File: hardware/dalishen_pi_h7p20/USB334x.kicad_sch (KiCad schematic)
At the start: 29 parts, among them J2 USB_C_Receptacle_USB2.0_16P, J3 USB_A, U18 LM2903, U19 LM2903, U2 LM2903, U20 USB3343, Y1 26M,NC

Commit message: [dalishen_pi_h7p20] backup
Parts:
- removed C2: 0.1uF, Capacitor_SMD:C_0402_1005Metric, symbol Device:C
- removed D5, D6: 1N5819(S4), vllogic:D_SOD-323_BAT60, symbol Device:D_Schottky
- removed R11: 0, Resistor_SMD:R_0402_1005Metric, symbol Device:R
- removed R88: 33, Resistor_SMD:R_0402_1005Metric, symbol Device:R
- C12, C14: value 20pF,NC -> 9pF
- J2: footprint Connector_USB:USB_C_Receptacle_GCT_USB4105-xx-A_16P_TopMnt_Horizontal -> vllogic:USB_C_Receptacle_16P
- J3: footprint vllogic:USB-AF-180 -> vllogic:USB-AF_YIJIAN
- R1, R79, R90: value 10k -> 10k,1%
- R78: value 1M,NC -> 1M
- U18, U19, U2: value LM2903 -> LM2903A-VR
- Y1: value 26M,NC -> 26M
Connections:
- net GND: now also J2.S1 (SHIELD), J3.5 (Shield)
- net VCC_3V3: now also R90.1; no longer C1.2, U18.8 (V+), U19.8 (V+), U2.8 (V+)
- net VCC_5V: now also C1.2, U18.8 (V+), U19.8 (V+), U2.8 (V+)
- net at C50.2, U20.15 (VDD33), U20.18 (ID): no longer R90.1

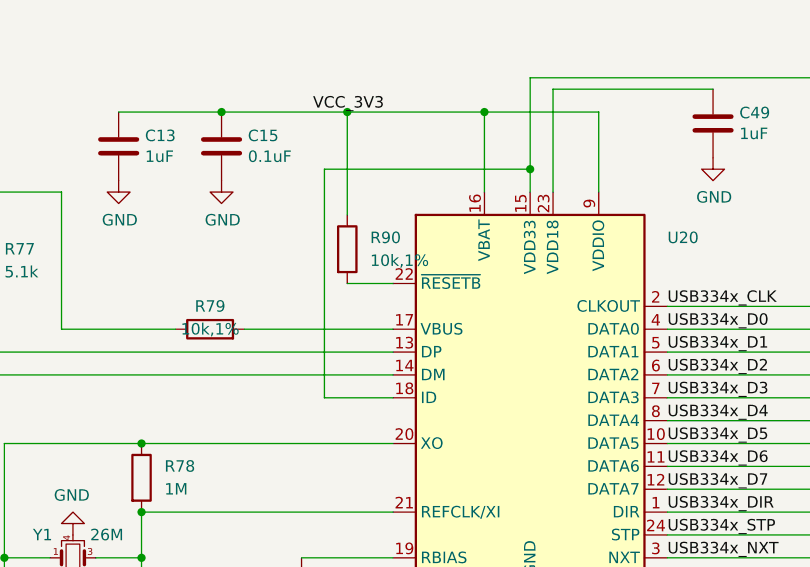
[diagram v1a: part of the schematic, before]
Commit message: [dalishen_pi_h7p20] 原理图初稿
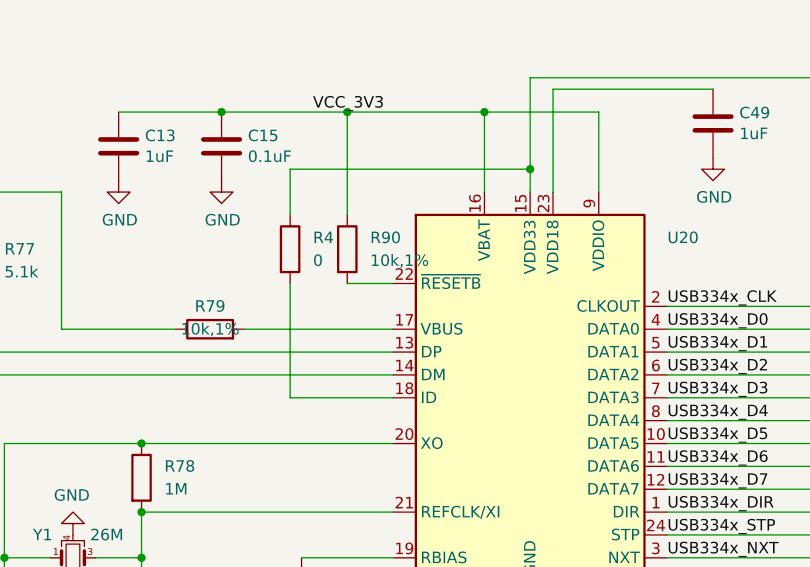
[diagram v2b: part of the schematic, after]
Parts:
- added R4: 0, Resistor_SMD:R_0402_1005Metric, symbol Device:R
- Y1: footprint vllogic:OSC_3225 -> vllogic:OSC_2016
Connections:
- net at C50.2, U20.15 (VDD33): now also R4.1; no longer U20.18 (ID)
- new net: R4.2, U20.18 (ID)
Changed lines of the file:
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@@
+    (stroke (width 0) (type default))
+  )
+  (wire (pts (xy 171.45 63.5) (xy 171.45 76.2))
     (stroke (width 0) (type default))
   )
@@
     (stroke (width 0) (type default))
   )
-  (wire (pts (xy 175.26 76.2) (xy 182.88 76.2))
+  (wire (pts (xy 171.45 76.2) (xy 182.88 76.2))
     (stroke (width 0) (type default))
   )
@@
     (stroke (width 0) (type default))
   )
-  (wire (pts (xy 175.26 50.8) (xy 175.26 76.2))
+  (wire (pts (xy 171.45 50.8) (xy 171.45 55.88))
     (stroke (width 0) (type default))
   )
@@
     (stroke (width 0) (type default))
   )
-  (wire (pts (xy 175.26 50.8) (xy 198.12 50.8))
+  (wire (pts (xy 171.45 50.8) (xy 198.12 50.8))
     (stroke (width 0) (type default))
   )
@@
     )
   )
+  (symbol (lib_id "Device:R") (at 171.45 59.69 0) (unit 1)
+    (in_bom yes) (on_board yes) (dnp no) (fields_autoplaced)
+    (property "Reference" "R4" (at 173.99 58.42 0)
+      (effects (font (size 1.27 1.27)) (justify left))
+    )
+    (property "Value" "0" (at 173.99 60.96 0)
+      (effects (font (size 1.27 1.27)) (justify left))
+    )
+    (property "Footprint" "Resistor_SMD:R_0402_1005Metric" (at 169.672 59.69 90)
+      (effects (font (size 1.27 1.27)) hide)
+    )
+    (property "Datasheet" "~" (at 171.45 59.69 0)
+      (effects (font (size 1.27 1.27)) hide)
+    )
+    (pin "2")
+    (pin "1")
+    (instances
+      (project "dalishen_pi_h7p20"
+        (path "/221176f3-b6da-4f04-afa6-f8c6dd49907a/c2e39904-e110-4fb2-9a78-c219110dbd62"
+          (reference "R4") (unit 1)
+        )
+      )
+    )
+  )
   (symbol (lib_id "power:GND") (at 24.13 125.73 0) (unit 1)
     (in_bom yes) (on_board yes) (dnp no)
@@
       (effects (font (size 1.27 1.27)) (justify left))
     )
-    (property "Footprint" "vllogic:OSC_3225" (at 147.32 93.98 0)
-      (effects (font (size 1.27 1.27)) hide)
-    )
+    (property "Footprint" "vllogic:OSC_2016" (at 147.32 93.98 0)
+      (effects (font (size 1.27 1.27)) hide)
+    )

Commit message: [dalishen_pi_h7p20] 原理图预审
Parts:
- C12, C14: value 9pF -> 4.3pF
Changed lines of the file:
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@@
       (effects (font (size 1.27 1.27)) (justify right))
     )
-    (property "Value" "9pF" (at 142.621 100.203 0)
+    (property "Value" "4.3pF" (at 142.621 100.203 0)
       (effects (font (size 1.27 1.27)) (justify right))
     )
@@
       (effects (font (size 1.27 1.27)) (justify right))
     )
-    (property "Value" "9pF" (at 157.861 100.203 0)
-      (effects (font (size 1.27 1.27)) (justify right))
-    )
+    (property "Value" "4.3pF" (at 157.861 100.203 0)
+      (effects (font (size 1.27 1.27)) (justify right))
+    )

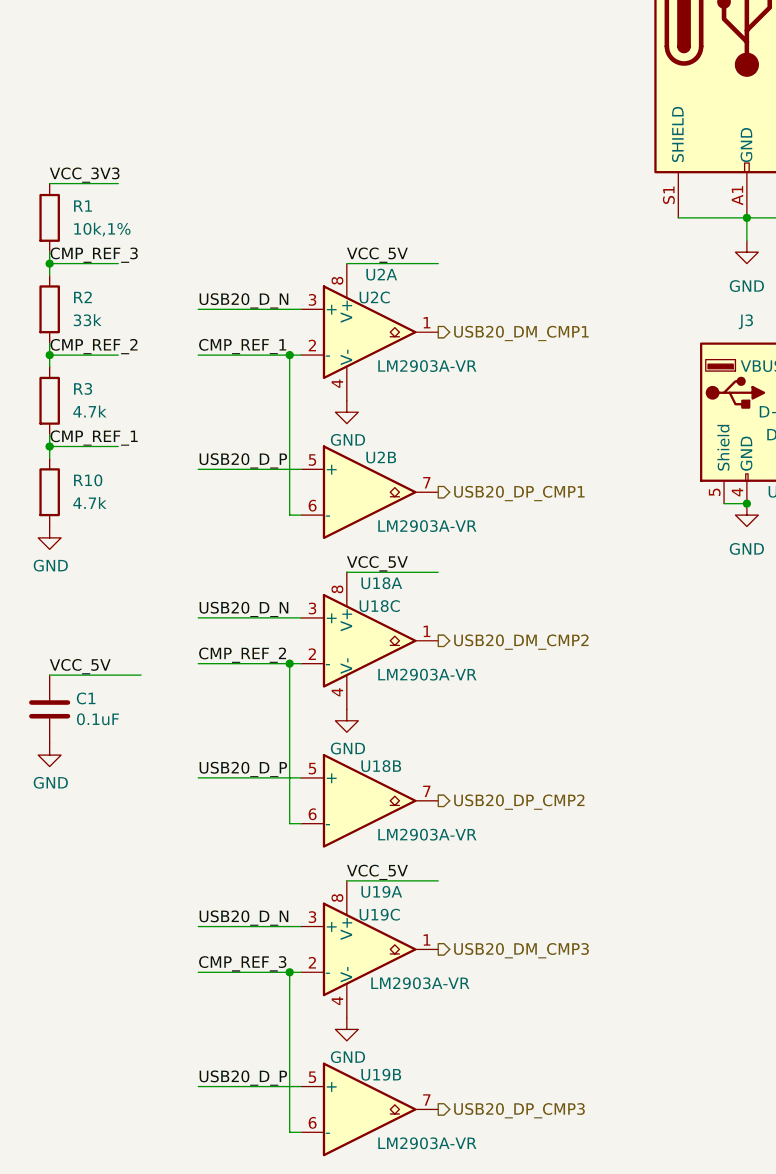
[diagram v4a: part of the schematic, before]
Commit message: [dalishen_pi_h7p20] 由于JTAG口在LQFP128封装上无法作为IO使用，故移除SE0，J, K状态电路
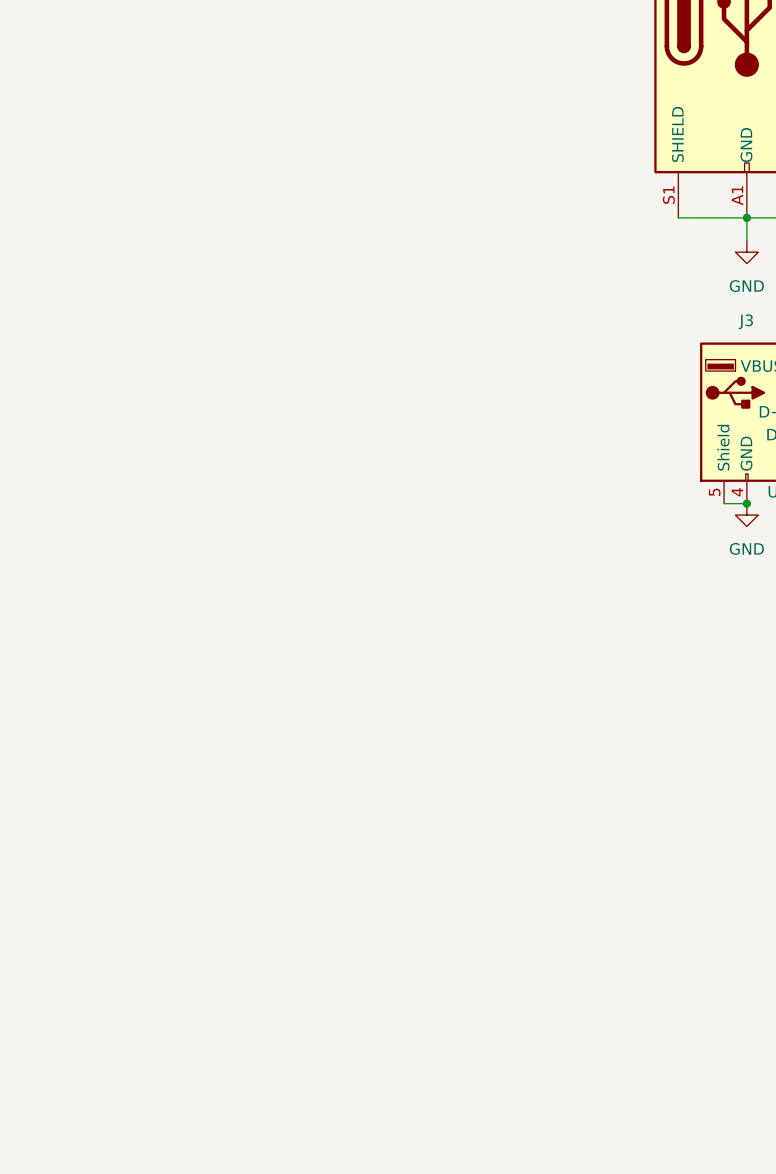
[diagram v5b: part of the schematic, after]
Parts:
- removed C1: 0.1uF, Capacitor_SMD:C_0402_1005Metric, symbol Device:C
- removed R1: 10k,1%, Resistor_SMD:R_0402_1005Metric, symbol Device:R
- removed R10, R3: 4.7k, Resistor_SMD:R_0402_1005Metric, symbol Device:R
- removed R2: 33k, Resistor_SMD:R_0402_1005Metric, symbol Device:R
- removed U18, U19, U2: LM2903A-VR, Package_SO:MSOP-8_3x3mm_P0.65mm, symbol Comparator:LM2903

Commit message: [dalishen_pi_h7p20] A母换SMT型号
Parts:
- J3: footprint vllogic:USB-AF_YIJIAN -> vllogic:USB_AF_SMT
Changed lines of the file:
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@@
 			)
 		)
-		(property "Footprint" "vllogic:USB-AF_YIJIAN"
+		(property "Footprint" "vllogic:USB_AF_SMT"
 			(at 105.41 114.3 0)
 			(effects
@@
 			)
 		)
-		(property "Datasheet" " ~"
+		(property "Datasheet" "~"
 			(at 105.41 114.3 0)
 			(effects

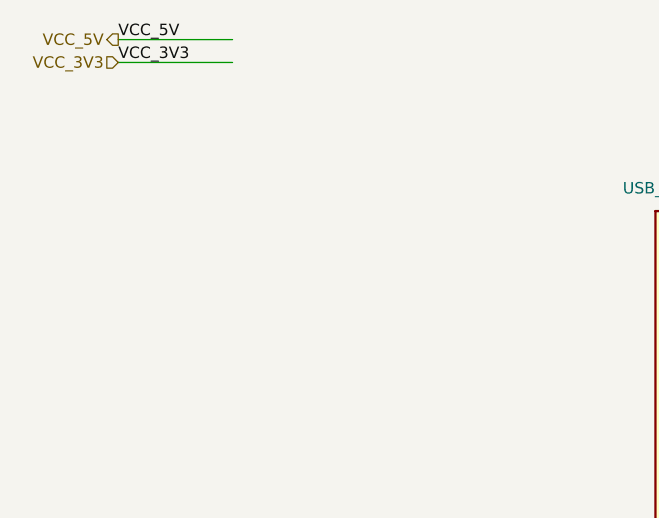
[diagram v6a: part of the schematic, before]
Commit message: [dalishen_pi_h7p20] 68013替换为双USB3343
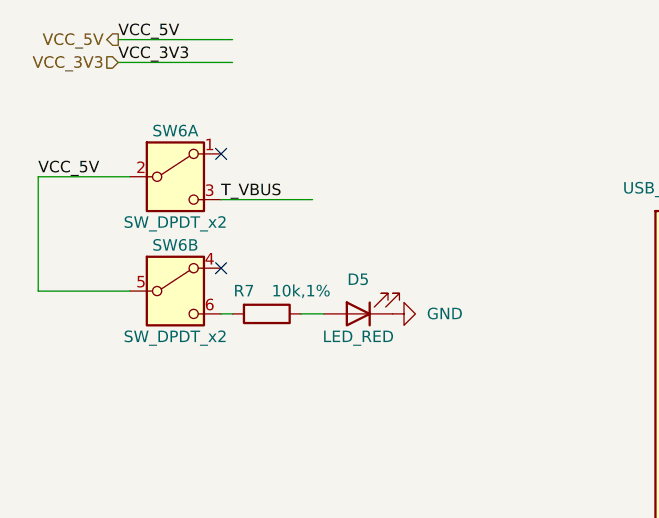
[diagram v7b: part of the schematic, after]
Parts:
- added D5: LED_RED, LED_SMD:LED_0603_1608Metric, symbol Device:LED
- added R7: 10k,1%, Resistor_SMD:R_0402_1005Metric, symbol Device:R
- added SW6: SW_DPDT_x2, symbol Switch:SW_DPDT_x2
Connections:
- net GND: now also D5.1 (K)
- net T_VBUS: now also SW6.3 (C)
- net VCC_5V: now also SW6.2 (B), SW6.5 (B)
- new net: D5.2 (A), R7.1
- new net: R7.2, SW6.6 (C)
- no-connect marks 0 -> 2
